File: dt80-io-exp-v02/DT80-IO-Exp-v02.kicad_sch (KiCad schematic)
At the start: 39 parts, among them J1 12V_IN, J10 DI2_IN, J11 UNI_A_V_mV_TC, J12 UNI_B_V_mV_TC, J13 4_20mA_LOOP, J14 RTD_PT100_PT1000, J15 SDI12_SENSOR, J16 RS485_MODBUS_SENSOR, J17 I2C_QWIIC_SENSOR, J18 1WIRE_SENSOR, J19 PULSE_FREQ_COUNT, J2 DT80_RS485, J3 AI1, J4 AI2, J5 AI3, J6 AI4, J7 REL1_OUT, J8 REL2_OUT, J9 DI1_IN, Q1 TLP281_DI1, Q2 TLP281_DI2, SW1 Modbus_ADDR, U1 MAX485, U2 ESP32-WROOM-32, U3 ADS1115, U4 ULN2003, U5 MP1584 12V-5V, U6 AMS1117-3.3

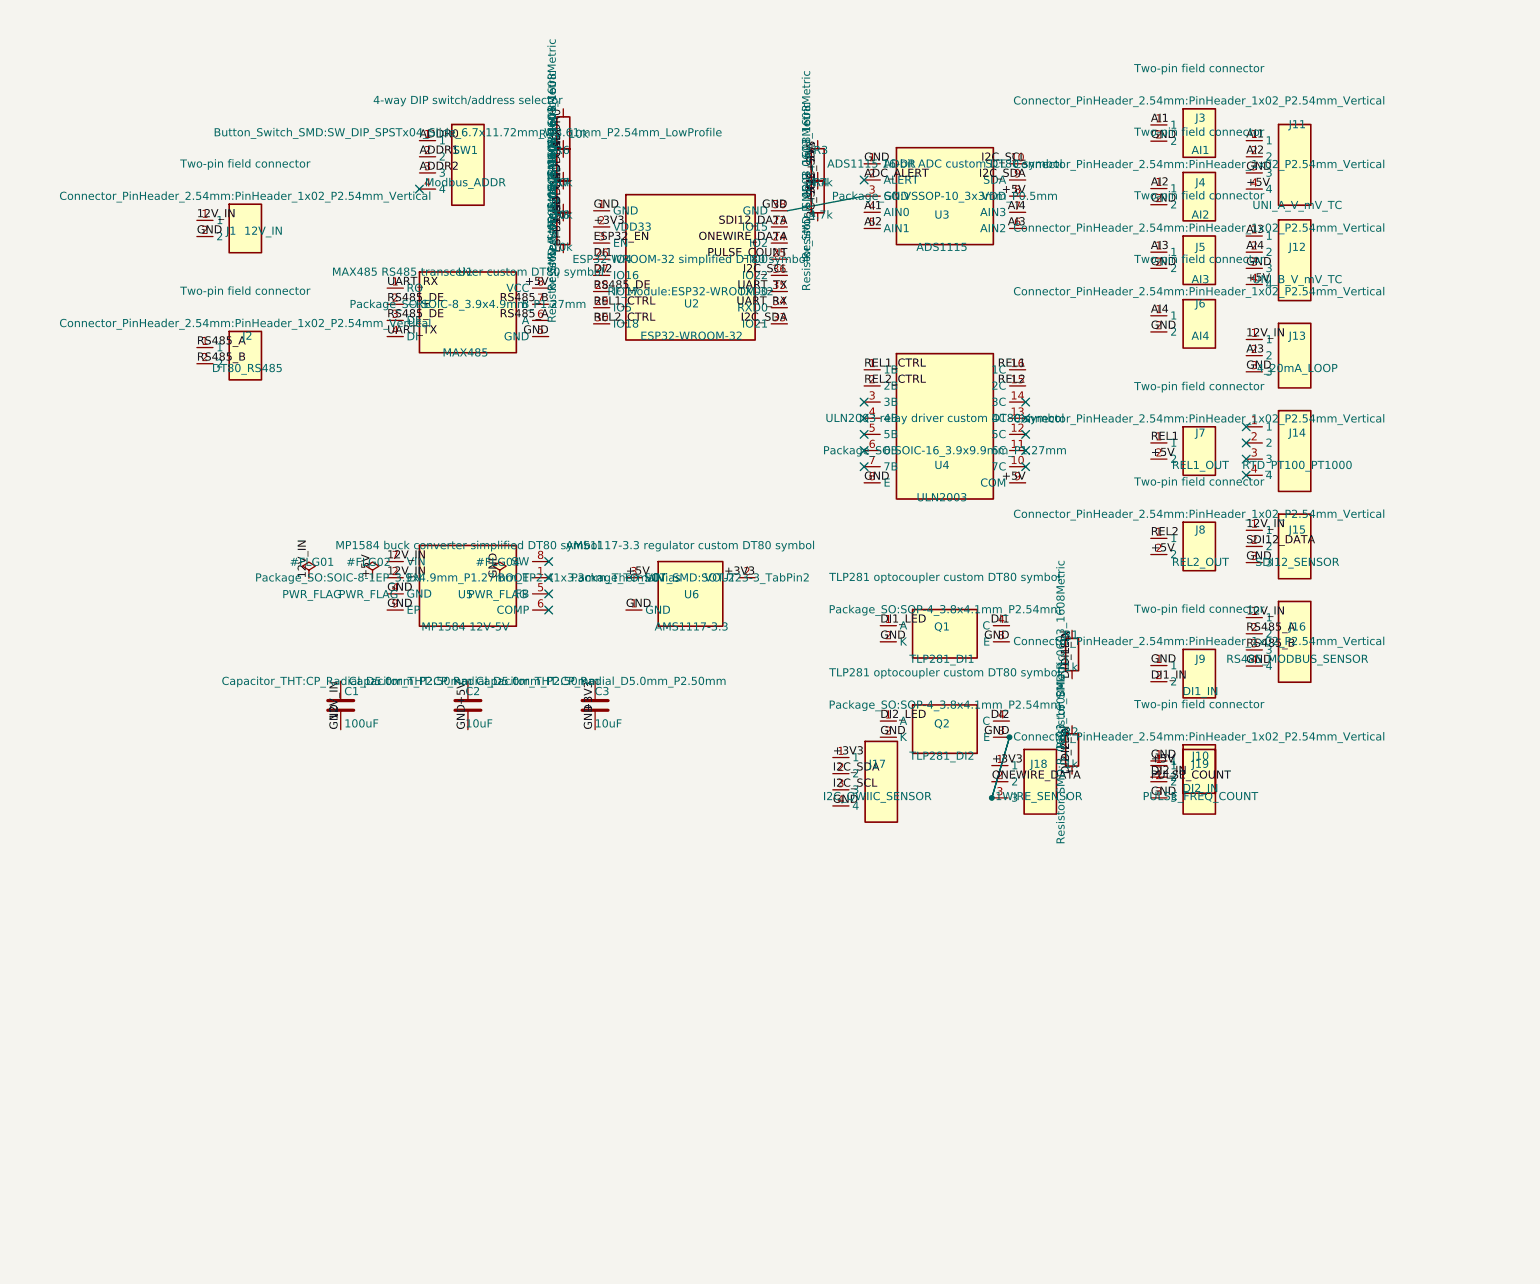
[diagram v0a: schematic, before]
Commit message: Add RTD BP loop and field protection frontends
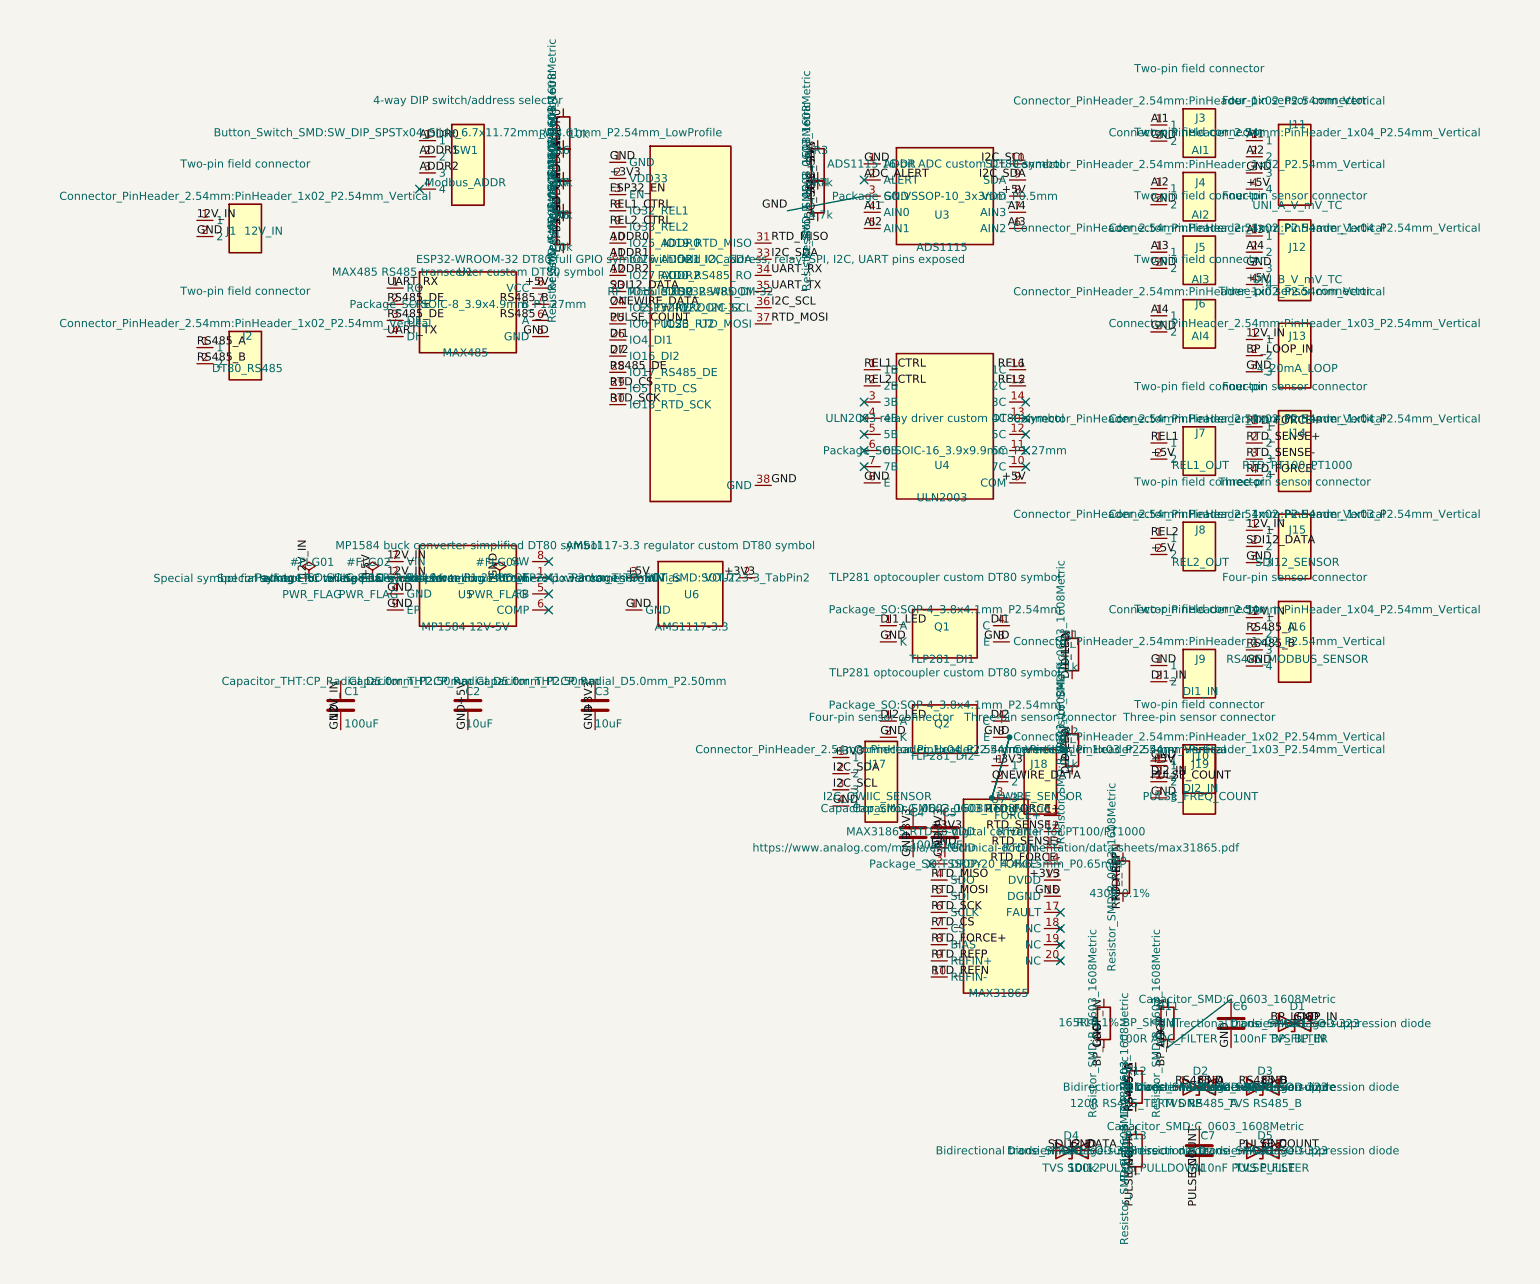
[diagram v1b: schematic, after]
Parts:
- removed U2: ESP32-WROOM-32, RF_Module:ESP32-WROOM-32, symbol DT80Custom:ESP32_WROOM32_DT80
- added C4: 100nF, Capacitor_SMD:C_0603_1608Metric, symbol Device:C
- added C5: 1uF, Capacitor_SMD:C_0603_1608Metric, symbol Device:C
- added C6: 100nF BP_FILTER, Capacitor_SMD:C_0603_1608Metric, symbol Device:C
- added C7: 10nF PULSE_FILTER, Capacitor_SMD:C_0603_1608Metric, symbol Device:C
- added D1: TVS BP_IN, Diode_SMD:D_SOD-323, symbol Device:D_TVS
- added D2: TVS RS485_A, Diode_SMD:D_SOD-323, symbol Device:D_TVS
- added D3: TVS RS485_B, Diode_SMD:D_SOD-323, symbol Device:D_TVS
- added D4: TVS SDI12, Diode_SMD:D_SOD-323, symbol Device:D_TVS
- added D5: TVS PULSE, Diode_SMD:D_SOD-323, symbol Device:D_TVS
- added R10: 165R 0.1% BP_SHUNT, Resistor_SMD:R_0603_1608Metric, symbol Device:R
- added R11: 100R ADC_FILTER, Resistor_SMD:R_0603_1608Metric, symbol Device:R
- added R12: 120R RS485_TERM DNP, Resistor_SMD:R_0603_1608Metric, symbol Device:R
- added R13: 100k PULSE_PULLDOWN, Resistor_SMD:R_0603_1608Metric, symbol Device:R
- added R9: 430R 0.1%, Resistor_SMD:R_0603_1608Metric, symbol Device:R
- added U2: ESP32-WROOM-32, RF_Module:ESP32-WROOM-32, symbol DT80Custom:ESP32_WROOM32_DT80_FULL
- added U7: MAX31865, Package_SO:TSSOP-20_4.4x6.5mm_P0.65mm, symbol DT80Custom:MAX31865_DT80
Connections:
- net +3V3: now also C4.1, C5.1, U2.2 (VDD33), U7.1 (VDD), U7.15 (DVDD)
- net ADDR0: now also U2.10 (IO25_ADDR0)
- net ADDR1: now also U2.11 (IO26_ADDR1)
- net ADDR2: now also U2.12 (IO27_ADDR2)
- net AI3: now also C6.1, R11.2; no longer J13.2
- net DI1: now also U2.26 (IO4_DI1)
- net DI2: now also U2.27 (IO16_DI2)
- net ESP32_EN: now also U2.3 (EN)
- net GND: now also C4.2, C5.2, C6.2, C7.2, D1.2 (A2), D2.2 (A2), D3.2 (A2), D4.2 (A2), D5.2 (A2), R10.2, R13.2, U2.1 (GND), U2.38 (GND), U7.16 (DGND), U7.2 (GND)
- net I2C_SCL: now also U2.36 (IO22_I2C_SCL)
- net I2C_SDA: now also U2.33 (IO21_I2C_SDA)
- net ONEWIRE_DATA: now also U2.24 (IO2_1WIRE)
- net PULSE_COUNT: now also C7.1, D5.1 (A1), R13.1, U2.25 (IO0_PULSE)
- net REL1_CTRL: now also U2.8 (IO32_REL1)
- net REL2_CTRL: now also U2.9 (IO33_REL2)
- net RS485_A: now also D2.1 (A1), R12.1
- net RS485_B: now also D3.1 (A1), R12.2
- net RS485_DE: now also U2.28 (IO17_RS485_DE)
- net SDI12_DATA: now also D4.1 (A1), U2.23 (IO15_SDI12)
- net UART_RX: now also U2.34 (RXD0_RS485_RO)
- net UART_TX: now also U2.35 (TXD0_RS485_DI)
- net RTD_FORCE+: now reaches J14.1
- net RTD_FORCE+: now also U7.11 (FORCE+), U7.8 (BIAS)
- net RTD_SENSE+: now reaches J14.2
- net RTD_SENSE+: now also U7.12 (RTDIN+)
- net RTD_SENSE-: now reaches J14.3
- net RTD_SENSE-: now also U7.13 (RTDIN-)
- net RTD_FORCE-: now reaches J14.4
- net RTD_FORCE-: now also U7.14 (FORCE-)
- new net BP_LOOP_IN: D1.1 (A1), J13.2, R10.1, R11.1
- new net RTD_CS: U2.29 (IO5_RTD_CS), U7.7 (CS)
- new net RTD_MISO: U2.31 (IO19_RTD_MISO), U7.4 (SDO)
- new net RTD_MOSI: U2.37 (IO23_RTD_MOSI), U7.5 (SDI)
- new net RTD_REFN: R9.2, U7.10 (REFIN-)
- new net RTD_REFP: R9.1, U7.9 (REFIN+)
- new net RTD_SCK: U2.30 (IO18_RTD_SCK), U7.6 (SCLK)
- no-connect marks 20 -> 21
